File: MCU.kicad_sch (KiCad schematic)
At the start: 29 parts, among them J3 Conn_ARM_SWD_TagConnect_TC2030, U1 MLPF-WB55-01E3, U5 STM32WB55CGUx, U7 MX25L3233FZN, X1 32MHz, X2 32kHz768

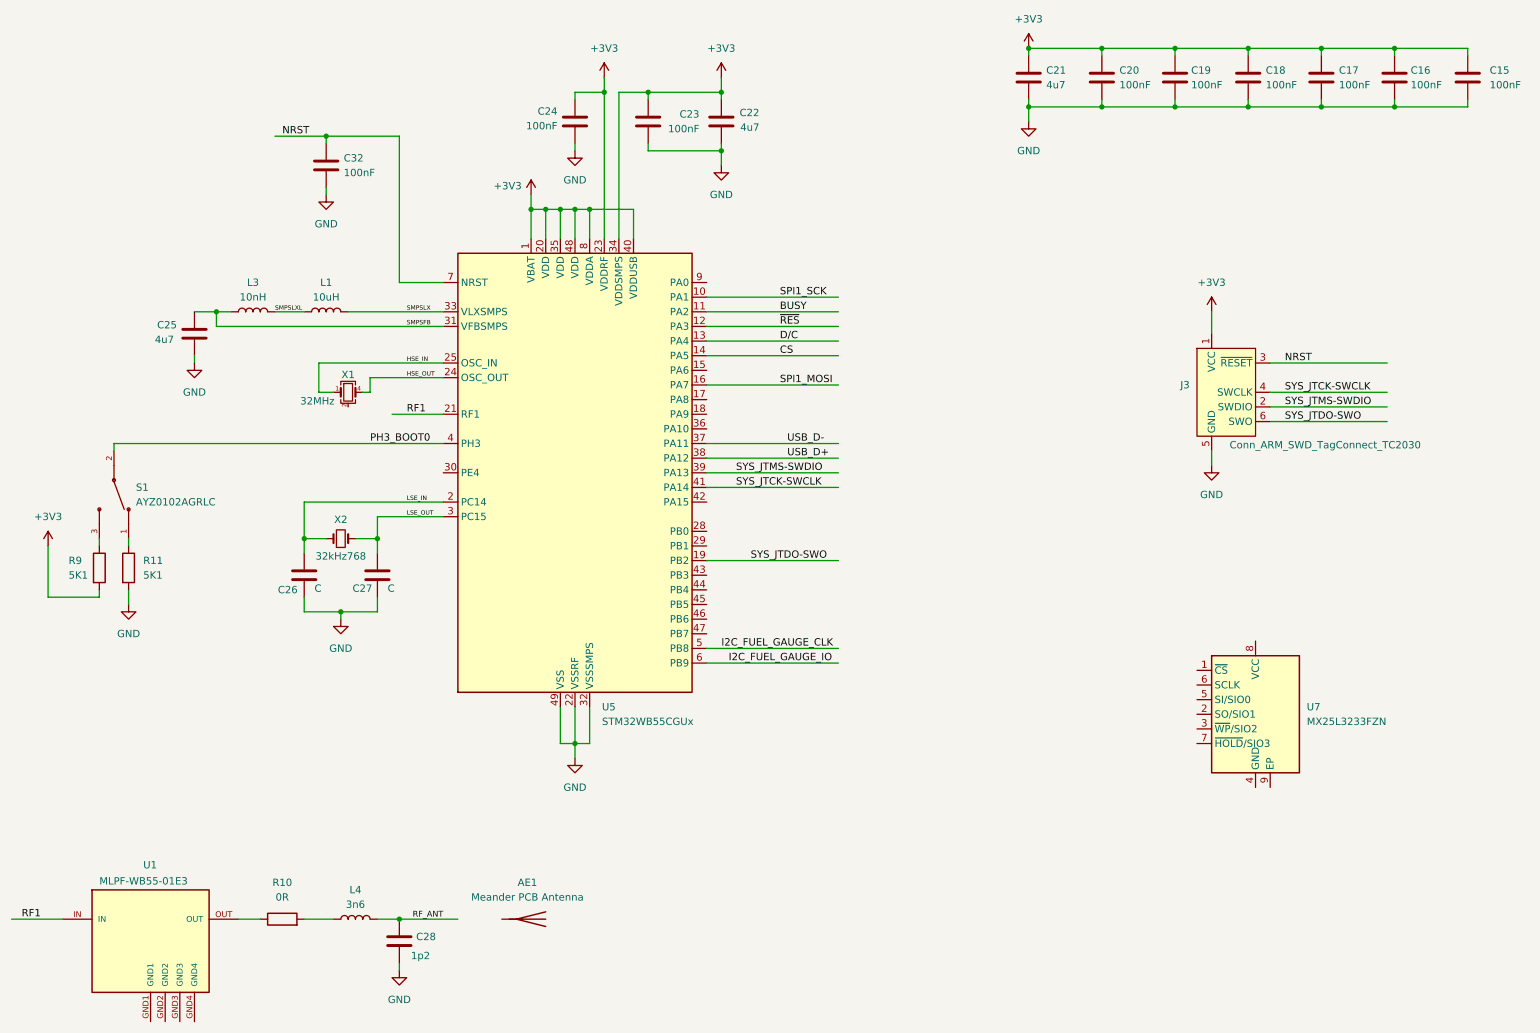
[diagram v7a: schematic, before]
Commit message: Added external flash ic & 4 push buttons
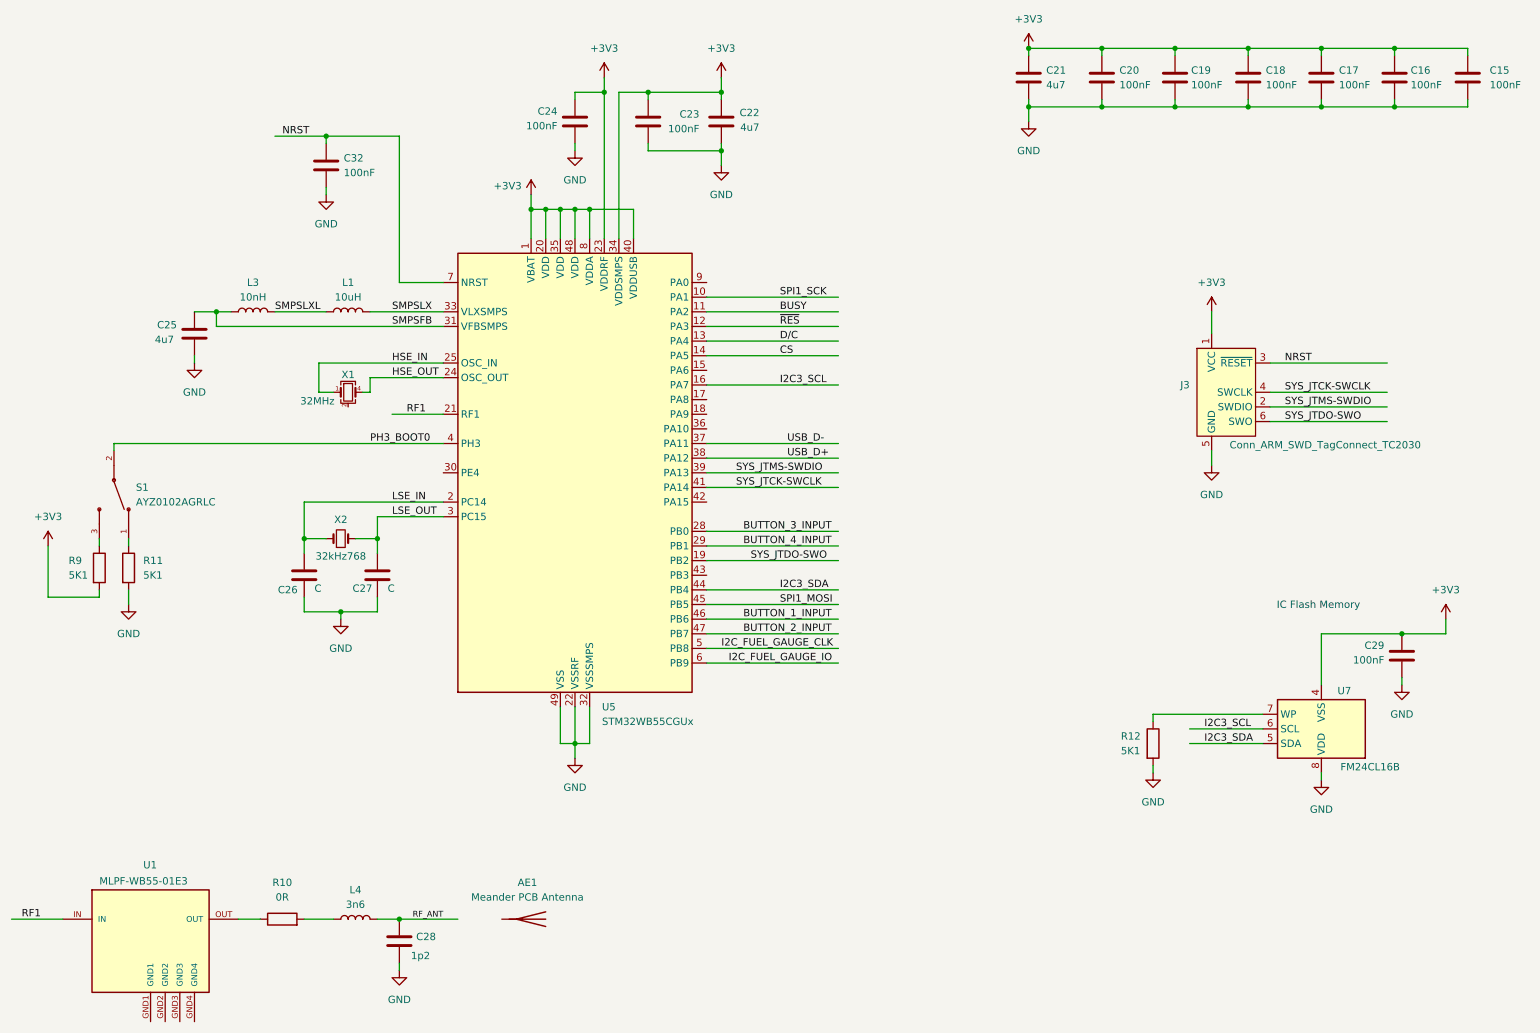
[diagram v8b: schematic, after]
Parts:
- removed U7: MX25L3233FZN, Package_SON:WSON-8-1EP_6x5mm_P1.27mm_EP3.4x4mm, symbol Memory_Flash:MX25L3233FZN
- added C29: 100nF, symbol Device:C
- added R12: 5K1, symbol Device:R
- added U7: FM24CL16B, Package_SO:SOIC-8_3.9x4.9mm_P1.27mm, symbol Memory_NVRAM:FM24CL16B
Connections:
- net +3V3: now also C29.1, U7.4 (VSS)
- net GND: now also C29.2, R12.2, U7.8 (VDD)
- net SPI1_MOSI: now also U5.45 (PB5); no longer U5.16 (PA7)
- net BUTTON_3_INPUT: now reaches U5.28 (PB0)
- net BUTTON_4_INPUT: now reaches U5.29 (PB1)
- net I2C3_SDA: now reaches U5.44 (PB4)
- net I2C3_SDA: now also U7.5 (SDA)
- net BUTTON_1_INPUT: now reaches U5.46 (PB6)
- net BUTTON_2_INPUT: now reaches U5.47 (PB7)
- new net: R12.1, U7.7 (WP)
- new net I2C3_SCL: U5.16 (PA7), U7.6 (SCL)
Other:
- note added: "IC Flash Memory"
- moved on the sheet: L1
